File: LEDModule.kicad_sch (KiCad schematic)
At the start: 11 parts

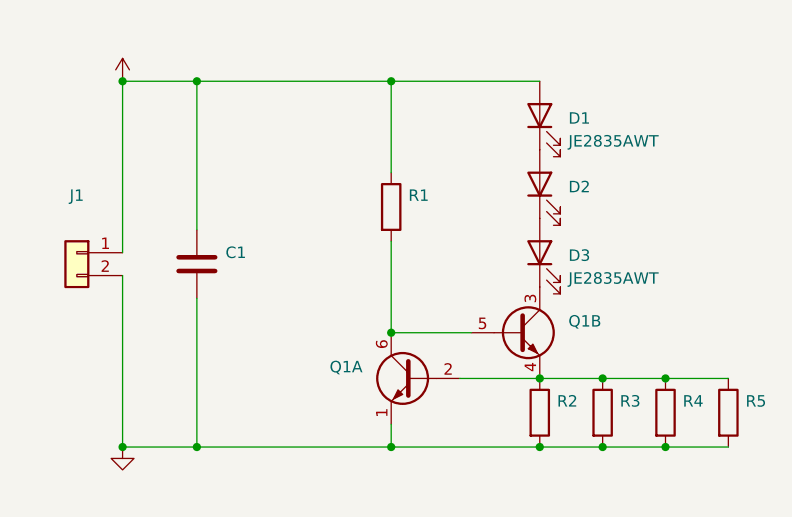
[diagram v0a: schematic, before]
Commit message: Updated package size of R1. Added LCSC BOM.
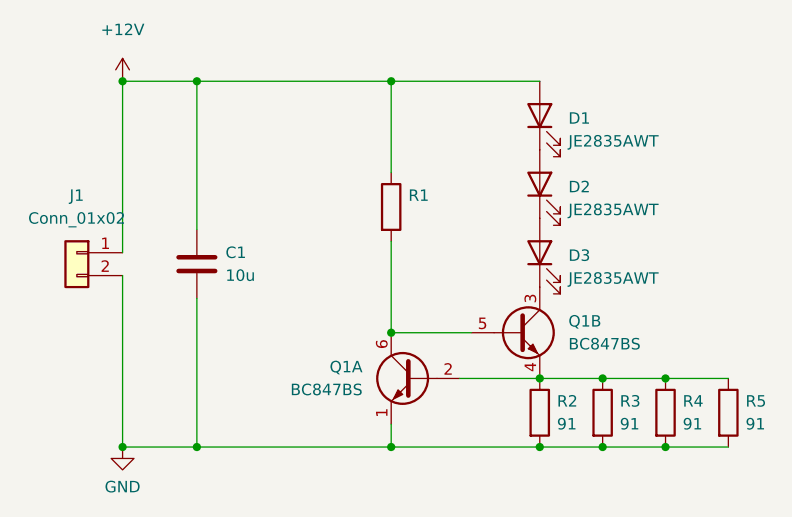
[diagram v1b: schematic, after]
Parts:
- C1: value (none) -> 10u; footprint (none) -> Capacitor_SMD:C_0805_2012Metric
- D2: value (none) -> JE2835AWT; footprint (none) -> Brett-Footprint:LED_Cree-J-Series
- J1: value (none) -> Conn_01x02; footprint (none) -> Brett-Footprint:TE-HPI-1x2x2mm-1775469-2
- Q1: value (none) -> BC847BS; footprint (none) -> Package_TO_SOT_SMD:SOT-363_SC-70-6
- R2, R3, R4, R5: value (none) -> 91; footprint (none) -> Resistor_SMD:R_1206_3216Metric
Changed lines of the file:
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@@
       (effects (font (size 1.27 1.27)) (justify left))
     )
-    (property "Value" "" (id 1) (at 107.95 146.6849 0)
-      (effects (font (size 1.27 1.27)) (justify left))
-    )
-    (property "Footprint" "" (id 2) (at 108.585 142.875 0)
+    (property "Value" "BC847BS" (id 1) (at 107.95 146.6849 0)
+      (effects (font (size 1.27 1.27)) (justify left))
+    )
+    (property "Footprint" "Package_TO_SOT_SMD:SOT-363_SC-70-6" (id 2) (at 108.585 142.875 0)
       (effects (font (size 1.27 1.27)) hide)
     )
@@
       (effects (font (size 1.27 1.27)) (justify left))
     )
-    (property "Value" "" (id 1) (at 130.81 141.6049 0)
-      (effects (font (size 1.27 1.27)) (justify left))
-    )
-    (property "Footprint" "" (id 2) (at 130.175 137.795 0)
+    (property "Value" "BC847BS" (id 1) (at 130.81 141.6049 0)
+      (effects (font (size 1.27 1.27)) (justify left))
+    )
+    (property "Footprint" "Package_TO_SOT_SMD:SOT-363_SC-70-6" (id 2) (at 130.175 137.795 0)
       (effects (font (size 1.27 1.27)) hide)
     )
@@
       (effects (font (size 1.27 1.27)) hide)
     )
-    (property "Value" "" (id 1) (at 81.28 157.48 0))
+    (property "Value" "GND" (id 1) (at 81.28 157.48 0))
     (property "Footprint" "" (id 2) (at 81.28 153.035 0)
       (effects (font (size 1.27 1.27)) hide)
@@
       (effects (font (size 1.27 1.27)) (justify left))
     )
-    (property "Value" "" (id 1) (at 150.495 150.4949 0)
-      (effects (font (size 1.27 1.27)) (justify left))
-    )
-    (property "Footprint" "" (id 2) (at 146.812 149.225 90)
+    (property "Value" "91" (id 1) (at 150.495 150.4949 0)
+      (effects (font (size 1.27 1.27)) (justify left))
+    )
+    (property "Footprint" "Resistor_SMD:R_1206_3216Metric" (id 2) (at 146.812 149.225 90)
       (effects (font (size 1.27 1.27)) hide)
     )
@@
       (effects (font (size 1.27 1.27)) hide)
     )
-    (property "Value" "" (id 1) (at 81.28 106.68 0))
+    (property "Value" "+12V" (id 1) (at 81.28 106.68 0))
     (property "Footprint" "" (id 2) (at 81.28 112.395 0)
       (effects (font (size 1.27 1.27)) hide)
@@
       (effects (font (size 1.27 1.27)) (justify right))
     )
-    (property "Value" "" (id 1) (at 130.81 126.6824 90)
-      (effects (font (size 1.27 1.27)) (justify right))
-    )
-    (property "Footprint" "" (id 2) (at 122.555 123.825 0)
+    (property "Value" "JE2835AWT" (id 1) (at 130.81 126.6824 90)
+      (effects (font (size 1.27 1.27)) (justify right))
+    )
+    (property "Footprint" "Brett-Footprint:LED_Cree-J-Series" (id 2) (at 122.555 123.825 0)
       (effects (font (size 1.27 1.27)) hide)
     )
@@
       (effects (font (size 1.27 1.27)) (justify left))
     )
-    (property "Value" "" (id 1) (at 129.54 150.4949 0)
-      (effects (font (size 1.27 1.27)) (justify left))
-    )
-    (property "Footprint" "" (id 2) (at 125.857 149.225 90)
+    (property "Value" "91" (id 1) (at 129.54 150.4949 0)
+      (effects (font (size 1.27 1.27)) (justify left))
+    )
+    (property "Footprint" "Resistor_SMD:R_1206_3216Metric" (id 2) (at 125.857 149.225 90)
       (effects (font (size 1.27 1.27)) hide)
     )
@@
       (effects (font (size 1.27 1.27)) (justify left))
     )
-    (property "Value" "" (id 1) (at 143.51 150.4949 0)
-      (effects (font (size 1.27 1.27)) (justify left))
-    )
-    (property "Footprint" "" (id 2) (at 139.827 149.225 90)
+    (property "Value" "91" (id 1) (at 143.51 150.4949 0)
+      (effects (font (size 1.27 1.27)) (justify left))
+    )
+    (property "Footprint" "Resistor_SMD:R_1206_3216Metric" (id 2) (at 139.827 149.225 90)
       (effects (font (size 1.27 1.27)) hide)
     )
@@
       (effects (font (size 1.27 1.27)) (justify left))
     )
-    (property "Value" "" (id 1) (at 92.71 133.9849 0)
-      (effects (font (size 1.27 1.27)) (justify left))
-    )
-    (property "Footprint" "" (id 2) (at 90.5002 136.525 0)
+    (property "Value" "10u" (id 1) (at 92.71 133.9849 0)
+      (effects (font (size 1.27 1.27)) (justify left))
+    )
+    (property "Footprint" "Capacitor_SMD:C_0805_2012Metric" (id 2) (at 90.5002 136.525 0)
       (effects (font (size 1.27 1.27)) hide)
     )
@@
     (in_bom yes) (on_board yes) (fields_autoplaced)
     (property "Reference" "J1" (id 0) (at 76.2 125.095 0))
-    (property "Value" "" (id 1) (at 76.2 127.635 0))
-    (property "Footprint" "" (id 2) (at 76.2 131.445 0)
+    (property "Value" "Conn_01x02" (id 1) (at 76.2 127.635 0))
+    (property "Footprint" "Brett-Footprint:TE-HPI-1x2x2mm-1775469-2" (id 2) (at 76.2 131.445 0)
       (effects (font (size 1.27 1.27)) hide)
     )
@@
       (effects (font (size 1.27 1.27)) (justify left))
     )
-    (property "Value" "" (id 1) (at 136.525 150.4949 0)
-      (effects (font (size 1.27 1.27)) (justify left))
-    )
-    (property "Footprint" "" (id 2) (at 132.842 149.225 90)
+    (property "Value" "91" (id 1) (at 136.525 150.4949 0)
+      (effects (font (size 1.27 1.27)) (justify left))
+    )
+    (property "Footprint" "Resistor_SMD:R_1206_3216Metric" (id 2) (at 132.842 149.225 90)
       (effects (font (size 1.27 1.27)) hide)
     )
@@
     )
     (path "/f53b9085-720d-423c-9974-6a8861a8f6e7"
-      (reference "R1") (unit 1) (value "R") (footprint "Resistor_SMD:R_0201_0603Metric")
+      (reference "R1") (unit 1) (value "100k") (footprint "Resistor_SMD:R_0603_1608Metric")
     )
     (path "/622dc6a6-e855-432b-b187-fbde5659e868"
